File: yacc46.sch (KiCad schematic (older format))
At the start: 127 parts, among them J1 USB_C_Receptacle_USB2.0, J2 OLED_I2C, J3 AVR-ISP-6, J4 GLOVE_I2C, J5 TRRS_I2C, SW1 SW_PUSH, SW10 SW_PUSH, SW11 SW_PUSH, SW12 SW_PUSH, SW13 SW_PUSH, SW14 SW_PUSH, SW15 SW_PUSH, SW16 SW_PUSH, SW17 SW_PUSH, SW18 SW_PUSH, SW19 Rotary_Encoder_Switch, SW2 SW_PUSH, SW20 SW_PUSH, SW21 SW_PUSH, SW22 SW_PUSH, SW23 SW_PUSH, SW24 SW_PUSH, SW25 SW_PUSH, SW26 SW_PUSH, SW27 SW_PUSH, SW28 SW_PUSH, SW29 SW_PUSH, SW3 SW_PUSH, SW30 SW_PUSH, SW31 SW_PUSH, SW32 SW_PUSH, SW33 SW_PUSH, SW34 SW_PUSH, SW35 SW_PUSH, SW36 Rotary_Encoder_Switch, SW37 SW_PUSH, SW38 SW_PUSH, SW39 SW_PUSH, SW4 SW_PUSH, SW40 SW_PUSH, SW41 SW_PUSH, SW42 SW_PUSH, SW43 SW_PUSH, SW44 SW_PUSH, SW45 SW_PUSH, SW46 SW_PUSH, SW47 SW_Push, SW5 SW_PUSH, SW6 SW_PUSH, SW7 SW_PUSH, SW8 SW_PUSH, SW9 SW_PUSH, U1 ATmega32U4-AU, Y1 16MHz

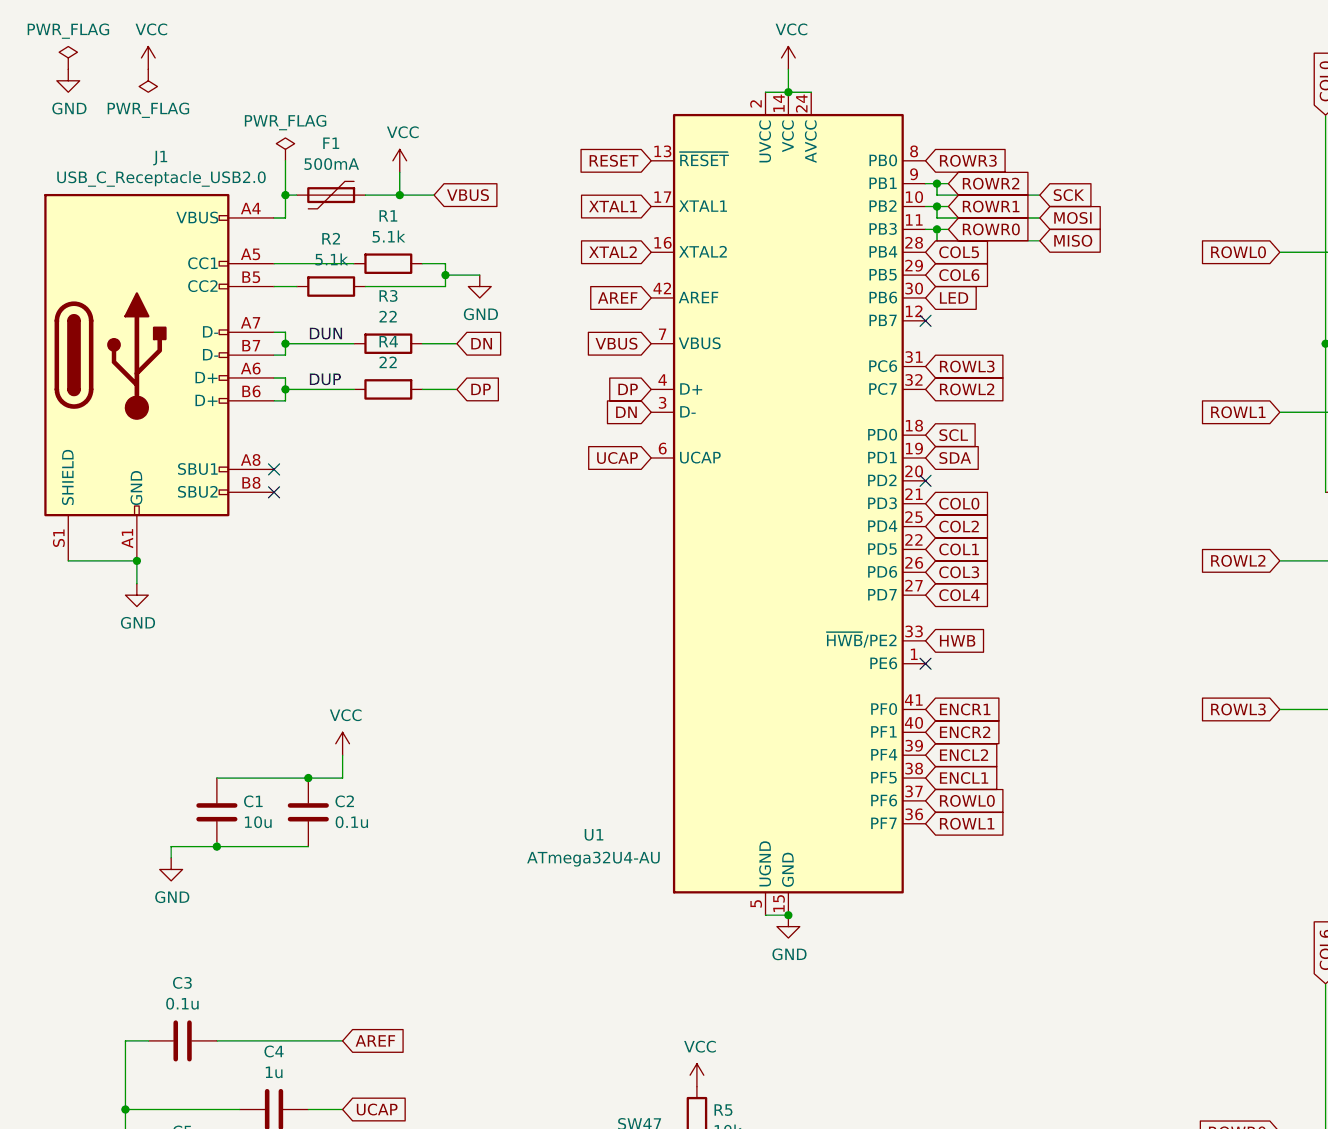
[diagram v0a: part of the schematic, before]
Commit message: USBコネクタをCX70M-24P1に変更
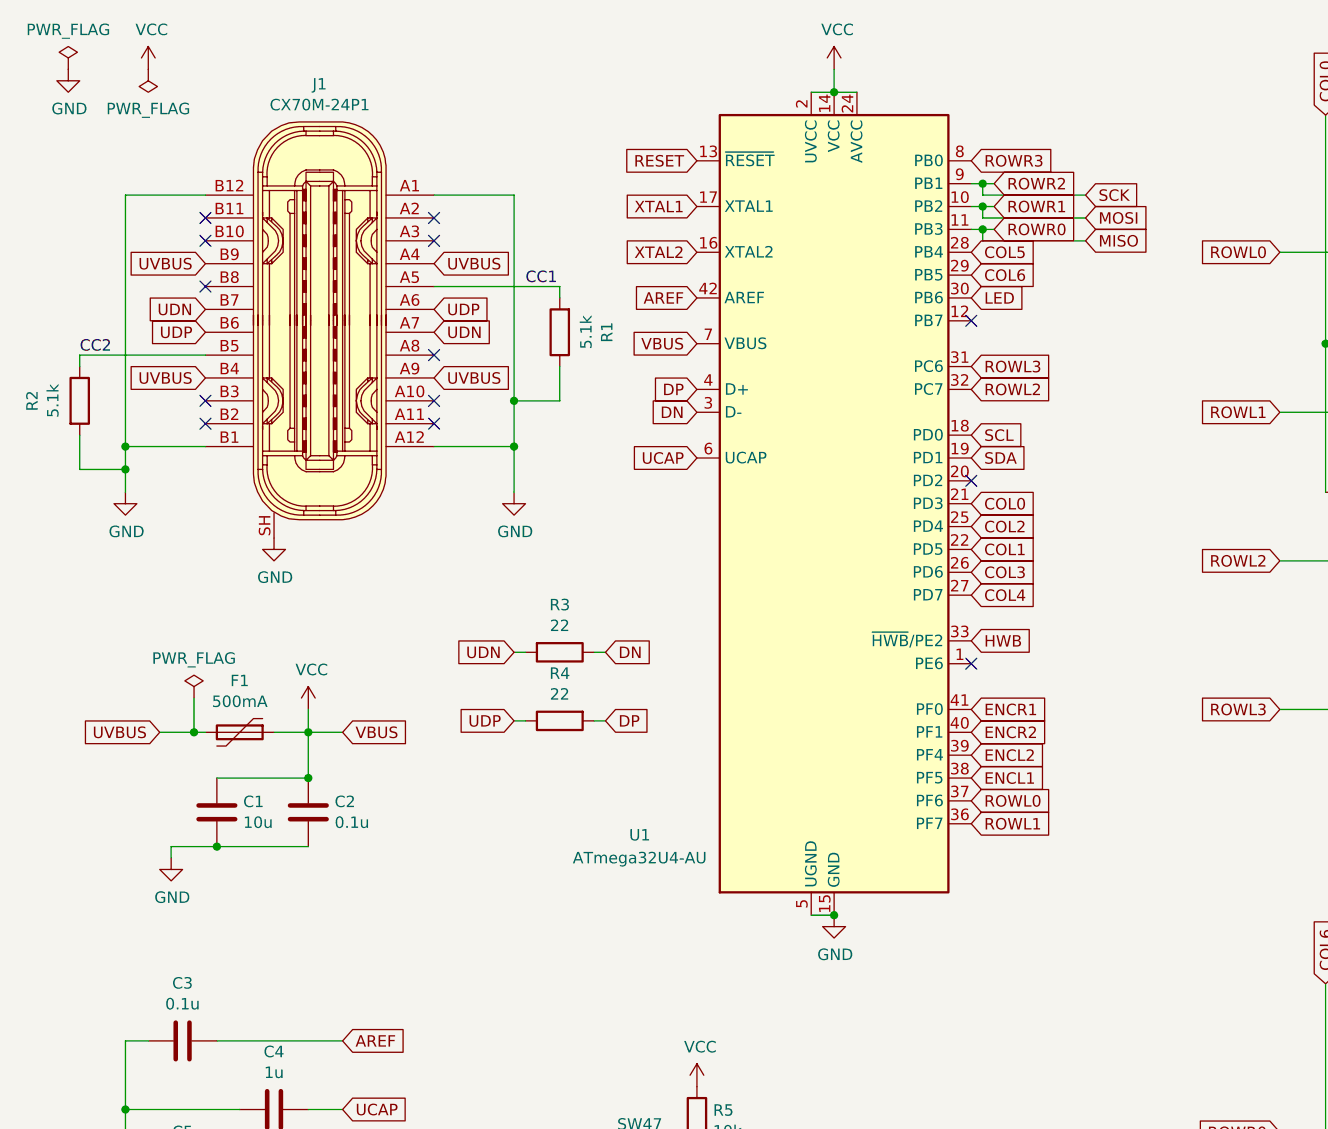
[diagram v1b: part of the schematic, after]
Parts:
- removed J1: USB_C_Receptacle_USB2.0, 1m38_kbd:USB_C_Receptacle_GCT_USB4085, symbol Connector:USB_C_Receptacle_USB2.0
- added J1: CX70M-24P1, digikey-footprints:USB-C_Female_CX70M-24P1, symbol dk_USB-DVI-HDMI-Connectors:CX70M-24P1
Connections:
- net GND: now also R2.2, J1.A1, J1.A12, J1.B1, J1.B12, J1.SH; no longer R2.1
- net UVBUS: now reaches F1.2
- net UVBUS: now also J1.A4, J1.A9, J1.B4, J1.B9
- net CC1: now reaches R1.2
- net CC1: now also J1.A5
- net DUN renamed UDN
- net UDN: now also J1.A7, J1.B7
- net DUP renamed UDP
- net UDP: now also J1.A6, J1.B6
- new net CC2: J1.B5, R2.1
- no-connect marks 20 -> 28
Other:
- moved on the sheet: F1, R1, R2, R3, R4, U1

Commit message: おおよそPCBの最終調整完了
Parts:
- R1, R2, R3, R4, R5, R6: footprint Resistor_SMD:R_0603_1608Metric_Pad1.05x0.95mm_HandSolder -> Resistor_SMD:R_0805_2012Metric_Pad1.15x1.40mm_HandSolder
- SW47: footprint foostan-kbd:ResetSW_1side -> 1m38_kbd:ResetSW_SKRPABE010
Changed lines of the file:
@@
 F 0 "R3" V 2743 3450 50  0000 C CNN
 F 1 "22" V 2834 3450 50  0000 C CNN
-F 2 "Resistor_SMD:R_0603_1608Metric_Pad1.05x0.95mm_HandSolder" V 2880 3450 50  0001 C CNN
+F 2 "Resistor_SMD:R_0805_2012Metric_Pad1.15x1.40mm_HandSolder" V 2880 3450 50  0001 C CNN
 F 3 "~" H 2950 3450 50  0001 C CNN
 	1    2950 3450
@@
 F 0 "R1" V 2743 2050 50  0000 C CNN
 F 1 "5.1k" V 2834 2050 50  0000 C CNN
-F 2 "Resistor_SMD:R_0603_1608Metric_Pad1.05x0.95mm_HandSolder" V 2880 2050 50  0001 C CNN
+F 2 "Resistor_SMD:R_0805_2012Metric_Pad1.15x1.40mm_HandSolder" V 2880 2050 50  0001 C CNN
 F 3 "~" H 2950 2050 50  0001 C CNN
 	1    2950 2050
@@
 F 0 "R5" H 3480 5546 50  0000 R CNN
 F 1 "10k" H 3480 5455 50  0000 R CNN
-F 2 "Resistor_SMD:R_0603_1608Metric_Pad1.05x0.95mm_HandSolder" V 3480 5500 50  0001 C CNN
+F 2 "Resistor_SMD:R_0805_2012Metric_Pad1.15x1.40mm_HandSolder" V 3480 5500 50  0001 C CNN
 F 3 "~" H 3550 5500 50  0001 C CNN
 	1    3550 5500
@@
 F 0 "SW47" H 3300 6085 50  0000 C CNN
 F 1 "SW_Push" H 3300 5994 50  0000 C CNN
-F 2 "foostan-kbd:ResetSW_1side" H 3300 6000 50  0001 C CNN
+F 2 "1m38_kbd:ResetSW_SKRPABE010" H 3300 6000 50  0001 C CNN
 F 3 "~" H 3300 6000 50  0001 C CNN
 	1    3300 5800
@@
 F 0 "R6" V 3093 6150 50  0000 C CNN
 F 1 "10k" V 3184 6150 50  0000 C CNN
-F 2 "Resistor_SMD:R_0603_1608Metric_Pad1.05x0.95mm_HandSolder" V 3230 6150 50  0001 C CNN
+F 2 "Resistor_SMD:R_0805_2012Metric_Pad1.15x1.40mm_HandSolder" V 3230 6150 50  0001 C CNN
 F 3 "~" H 3300 6150 50  0001 C CNN
 	1    3300 6150
@@
 F 0 "R4" V 2743 3750 50  0000 C CNN
 F 1 "22" V 2834 3750 50  0000 C CNN
-F 2 "Resistor_SMD:R_0603_1608Metric_Pad1.05x0.95mm_HandSolder" V 2880 3750 50  0001 C CNN
+F 2 "Resistor_SMD:R_0805_2012Metric_Pad1.15x1.40mm_HandSolder" V 2880 3750 50  0001 C CNN
 F 3 "~" H 2950 3750 50  0001 C CNN
 	1    2950 3750
@@
 $EndComp
 $Comp
-L power:GND #PWR?
+L power:GND #PWR0105
 U 1 1 5F65FD44
 P 1700 2950
-F 0 "#PWR?" H 1700 2700 50  0001 C CNN
+F 0 "#PWR0105" H 1700 2700 50  0001 C CNN
 F 1 "GND" H 1705 2777 50  0000 C CNN
 F 2 "" H 1700 2950 50  0001 C CNN
@@
 $EndComp
 $Comp
-L power:GND #PWR?
+L power:GND #PWR0106
 U 1 1 5F660277
 P 1050 2750
-F 0 "#PWR?" H 1050 2500 50  0001 C CNN
+F 0 "#PWR0106" H 1050 2500 50  0001 C CNN
 F 1 "GND" H 1055 2577 50  0000 C CNN
 F 2 "" H 1050 2750 50  0001 C CNN
@@
 	1050 2550 1050 2650
 $Comp
-L power:GND #PWR?
+L power:GND #PWR0107
 U 1 1 5F6A04EF
 P 2750 2750
-F 0 "#PWR?" H 2750 2500 50  0001 C CNN
+F 0 "#PWR0107" H 2750 2500 50  0001 C CNN
 F 1 "GND" H 2755 2577 50  0000 C CNN
 F 2 "" H 2750 2750 50  0001 C CNN
@@
 F 0 "R2" V 643 2350 50  0000 C CNN
 F 1 "5.1k" V 734 2350 50  0000 C CNN
-F 2 "Resistor_SMD:R_0603_1608Metric_Pad1.05x0.95mm_HandSolder" V 780 2350 50  0001 C CNN
+F 2 "Resistor_SMD:R_0805_2012Metric_Pad1.15x1.40mm_HandSolder" V 780 2350 50  0001 C CNN
 F 3 "~" H 850 2350 50  0001 C CNN
 	1    850  2350
